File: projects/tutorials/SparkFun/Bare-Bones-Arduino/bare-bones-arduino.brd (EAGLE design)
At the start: 160 x 100 mm, 15 parts, among them J1 POWER_JACK, J2 AVR_SPI_PROG_3X2PTH, J3 HEADER1x06, J4 HEADER1X08, U1 328P

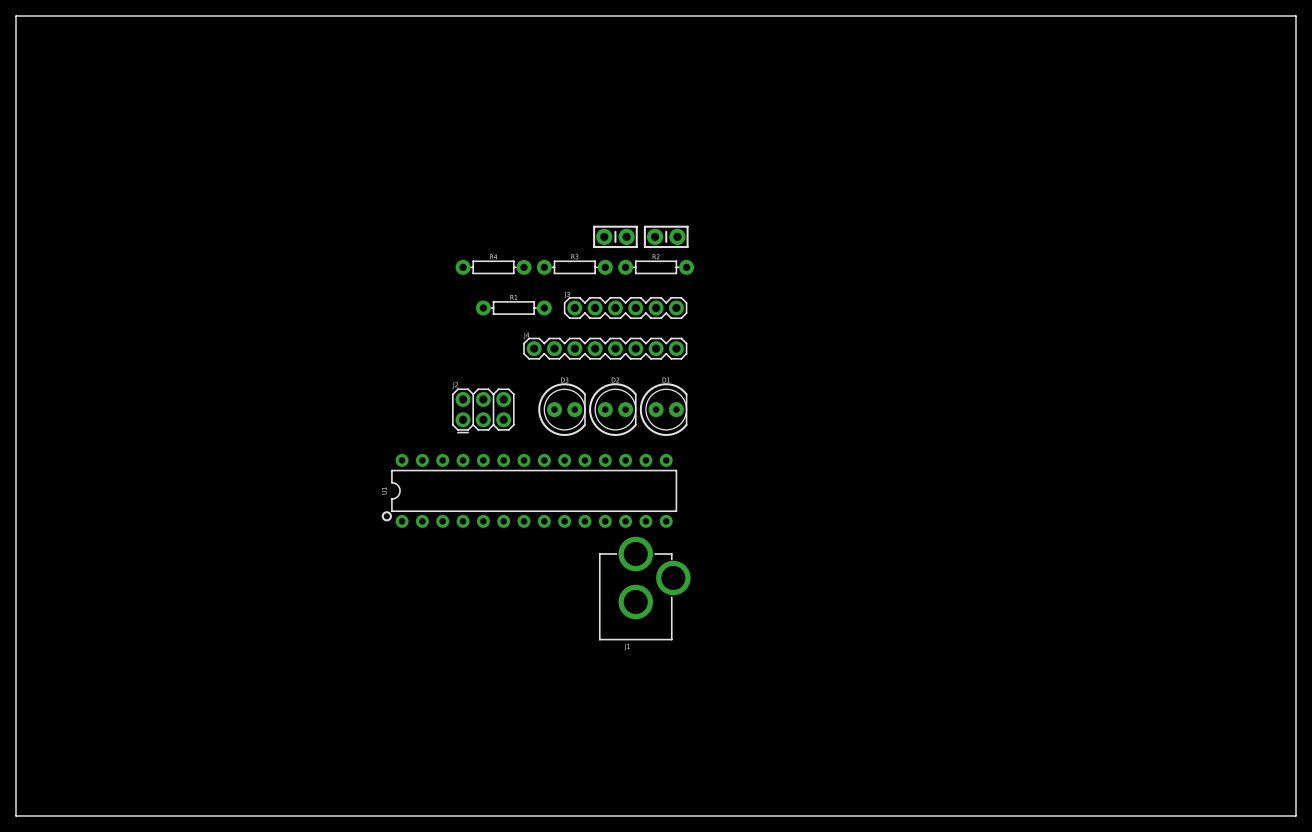
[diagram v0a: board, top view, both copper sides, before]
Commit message: First stab at component placement for barebones Arduino board
Signed-off-by: Naveed Kawsar <naveedkawsar@outlook.com>
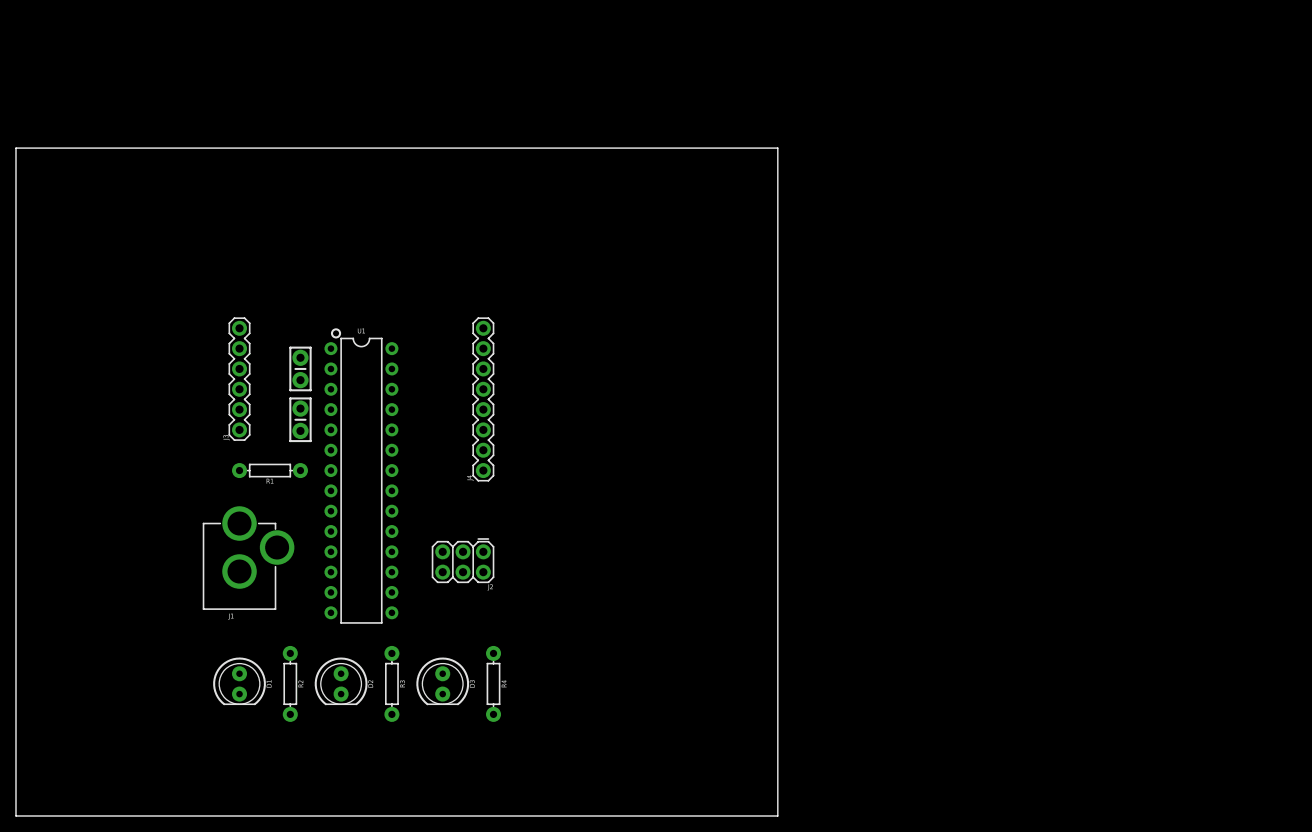
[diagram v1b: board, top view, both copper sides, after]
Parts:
- moved R2 69.3 mm to (34.3, 16.5), turned to 270 degrees
- moved D1 63.4 mm to (27.9, 16.5), turned to 270 degrees
- moved R3 56.9 mm to (47.0, 16.5), turned to 270 degrees
- moved R4 52.1 mm to (59.7, 16.5), turned to 270 degrees
- moved J1 49.7 mm to (27.9, 22.9)
- moved C1 48.6 mm to (35.6, 55.9), turned to 270 degrees
- moved D2 48.5 mm to (40.6, 16.5), turned to 270 degrees
- moved C2 45.5 mm to (35.6, 49.5), turned to 270 degrees
- moved J3 44.6 mm to (27.9, 48.3), turned to 90 degrees
- moved FRAME1 44.5 mm to (35.6, 45.7), turned to 90 degrees
- moved D3 37.5 mm to (53.3, 16.5), turned to 270 degrees
- moved R1 36.6 mm to (31.8, 43.2), turned to 180 degrees
- moved U1 21.6 mm to (43.2, 41.9), turned to 270 degrees
- moved J2 16.7 mm to (58.4, 33.0), turned to 180 degrees
- moved J4 16.5 mm to (58.4, 43.2), turned to 90 degrees
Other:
- board size 160 x 100 mm -> 95.2 x 83.5 mm
